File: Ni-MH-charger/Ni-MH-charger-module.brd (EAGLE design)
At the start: 12 parts

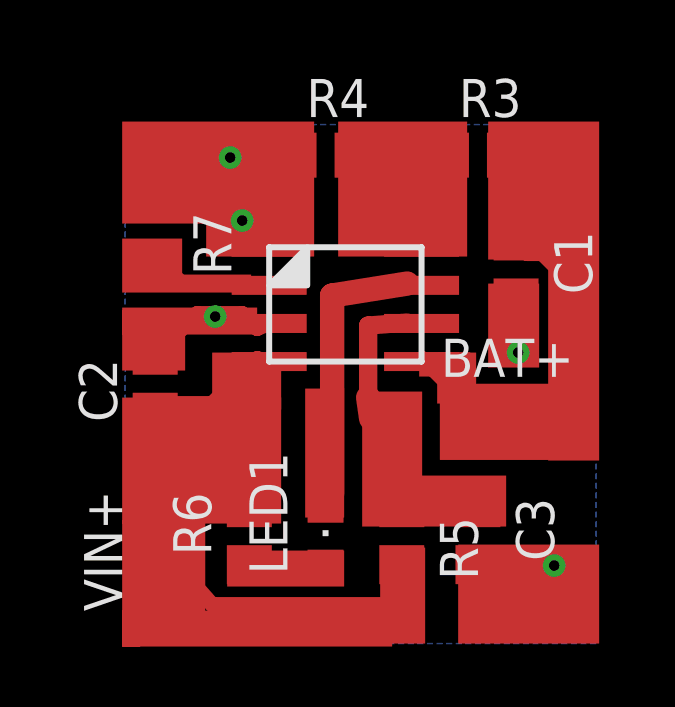
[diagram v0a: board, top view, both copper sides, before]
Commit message: Ni-MH-charger updated
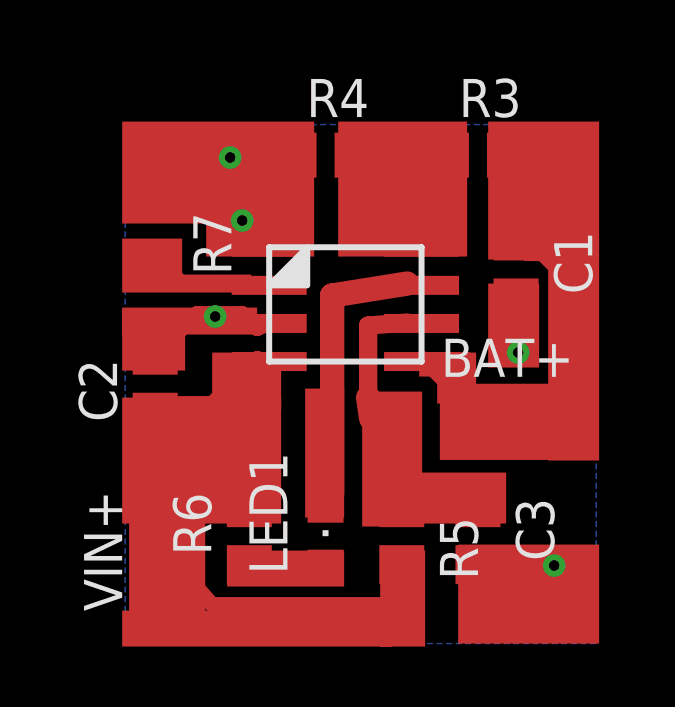
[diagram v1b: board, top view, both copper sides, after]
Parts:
- C3: value 100nf(?) - 133sec -> 100n(135s) 1u(22min)
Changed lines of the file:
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@@
 <layer number="19" name="Unrouted" color="6" fill="1" visible="no" active="yes"/>
 <layer number="20" name="Dimension" color="24" fill="1" visible="no" active="yes"/>
-<layer number="21" name="tPlace" color="7" fill="1" visible="no" active="yes"/>
+<layer number="21" name="tPlace" color="7" fill="1" visible="yes" active="yes"/>
 <layer number="22" name="bPlace" color="7" fill="1" visible="no" active="yes"/>
 <layer number="23" name="tOrigins" color="15" fill="1" visible="no" active="yes"/>
 <layer number="24" name="bOrigins" color="15" fill="1" visible="no" active="yes"/>
-<layer number="25" name="tNames" color="7" fill="1" visible="no" active="yes"/>
+<layer number="25" name="tNames" color="7" fill="1" visible="yes" active="yes"/>
 <layer number="26" name="bNames" color="7" fill="1" visible="no" active="yes"/>
 <layer number="27" name="tValues" color="7" fill="1" visible="no" active="yes"/>
@@
 <layer number="35" name="tGlue" color="7" fill="4" visible="no" active="yes"/>
 <layer number="36" name="bGlue" color="7" fill="5" visible="no" active="yes"/>
-<layer number="37" name="tTest" color="7" fill="1" visible="no" active="yes"/>
+<layer number="37" name="tTest" color="7" fill="1" visible="yes" active="yes"/>
 <layer number="38" name="bTest" color="7" fill="1" visible="no" active="yes"/>
 <layer number="39" name="tKeepout" color="4" fill="11" visible="no" active="yes"/>
@@
 <layer number="49" name="Reference" color="7" fill="1" visible="no" active="yes"/>
 <layer number="50" name="dxf" color="7" fill="1" visible="no" active="yes"/>
-<layer number="51" name="tDocu" color="7" fill="1" visible="no" active="yes"/>
+<layer number="51" name="tDocu" color="7" fill="1" visible="yes" active="yes"/>
 <layer number="52" name="bDocu" color="7" fill="1" visible="no" active="yes"/>
 <layer number="53" name="tGND_GNDA" color="7" fill="9" visible="no" active="no"/>
@@
 <rectangle x1="25.2" y1="7.6" x2="26.9" y2="14.3" layer="1"/>
 <rectangle x1="22.2" y1="1.5" x2="26.9" y2="4.8" layer="1"/>
-<rectangle x1="19.6" y1="5.4" x2="23.8" y2="7.1" layer="1"/>
-<rectangle x1="19.6" y1="1.5" x2="21.1" y2="4.7" layer="1"/>
-<rectangle x1="11" y1="1.4" x2="11.6" y2="5.6" layer="1"/>
+<rectangle x1="19.6" y1="5.5" x2="23.8" y2="7.2" layer="1"/>
+<rectangle x1="19.6" y1="1.4" x2="21.1" y2="4.6" layer="1"/>
+<rectangle x1="11.5" y1="1.8" x2="12.1" y2="6" layer="1"/>
 <rectangle x1="11" y1="1.4" x2="20" y2="2.6" layer="1"/>
 <rectangle x1="23.2" y1="10.7" x2="24.9" y2="13.5" layer="1"/>
@@
 <element name="C2" library="resistor" library_urn="urn:adsk.eagle:library:348" package="C0805" package3d_urn="urn:adsk.eagle:package:26137/1" value="10uf" x="12.1" y="10.16" rot="R90"/>
 <element name="BAT+" library="wirepad" library_urn="urn:adsk.eagle:library:412" package="SMD2,54-5,08" package3d_urn="urn:adsk.eagle:package:30841/1" value="" x="24.13" y="8.89" rot="R270"/>
-<element name="C3" library="resistor" library_urn="urn:adsk.eagle:library:348" package="C0805" package3d_urn="urn:adsk.eagle:package:26137/1" value="100nf(?) - 133sec" x="22.86" y="5.08" rot="R270"/>
+<element name="C3" library="resistor" library_urn="urn:adsk.eagle:library:348" package="C0805" package3d_urn="urn:adsk.eagle:package:26137/1" value="100n(135s) 1u(22min)" x="22.86" y="5.08" rot="R270"/>
 <element name="VIN+" library="wirepad" library_urn="urn:adsk.eagle:library:412" package="SMD2,54-5,08" package3d_urn="urn:adsk.eagle:package:30841/1" value="" x="12.5" y="5.08"/>
 <element name="LED1" library="adafruit" package="CHIPLED_0805" value="" x="17.78" y="5.08"/>

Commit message: Ni-MH-charger updates
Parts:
- C3: value 100n(135s) 1u(22min) -> 10uf
- R5: value 510k -> 750k
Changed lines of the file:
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@@
 <element name="R3" library="resistor" library_urn="urn:adsk.eagle:library:348" package="R0805" package3d_urn="urn:adsk.eagle:package:26059/1" value="24.9k - 1.5v" x="22.86" y="17.78"/>
 <element name="R4" library="resistor" library_urn="urn:adsk.eagle:library:348" package="R0805" package3d_urn="urn:adsk.eagle:package:26059/1" value="100k" x="17.78" y="17.78"/>
-<element name="R5" library="resistor" library_urn="urn:adsk.eagle:library:348" package="R0805" package3d_urn="urn:adsk.eagle:package:26059/1" value="510k" x="20.32" y="5.08" rot="R270"/>
+<element name="R5" library="resistor" library_urn="urn:adsk.eagle:library:348" package="R0805" package3d_urn="urn:adsk.eagle:package:26059/1" value="750k" x="20.32" y="5.08" rot="R270"/>
 <element name="R6" library="resistor" library_urn="urn:adsk.eagle:library:348" package="R0805" package3d_urn="urn:adsk.eagle:package:26059/1" value="330-4.7k(?)" x="15.24" y="5.08" rot="R90"/>
 <element name="R7" library="resistor" library_urn="urn:adsk.eagle:library:348" package="R0805" package3d_urn="urn:adsk.eagle:package:26059/1" value="1.21k(1A);1.5k(0.8A);2.4k(0.5A);12.1k(0.1A)" x="12.1" y="15.24" rot="R270"/>
@@
 <element name="C2" library="resistor" library_urn="urn:adsk.eagle:library:348" package="C0805" package3d_urn="urn:adsk.eagle:package:26137/1" value="10uf" x="12.1" y="10.16" rot="R90"/>
 <element name="BAT+" library="wirepad" library_urn="urn:adsk.eagle:library:412" package="SMD2,54-5,08" package3d_urn="urn:adsk.eagle:package:30841/1" value="" x="24.13" y="8.89" rot="R270"/>
-<element name="C3" library="resistor" library_urn="urn:adsk.eagle:library:348" package="C0805" package3d_urn="urn:adsk.eagle:package:26137/1" value="100n(135s) 1u(22min)" x="22.86" y="5.08" rot="R270"/>
+<element name="C3" library="resistor" library_urn="urn:adsk.eagle:library:348" package="C0805" package3d_urn="urn:adsk.eagle:package:26137/1" value="10uf" x="22.86" y="5.08" rot="R270"/>
 <element name="VIN+" library="wirepad" library_urn="urn:adsk.eagle:library:412" package="SMD2,54-5,08" package3d_urn="urn:adsk.eagle:package:30841/1" value="" x="12.5" y="5.08"/>
 <element name="LED1" library="adafruit" package="CHIPLED_0805" value="" x="17.78" y="5.08"/>
